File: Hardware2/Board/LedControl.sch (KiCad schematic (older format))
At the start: 47 parts, among them J2 Jumper, J3 Jumper, P1 USB_OTG, P10 TP, P11 2059-302, P12 DISPLAY, P13 TP, P14 Conn_01x03, P15 TP, P16 2059-302, P17 2059-302, P18 CONN_01X03, P19 CONN_01X03, P2 TP, P3 TP, P32 TP, P33 TP, P4 TP, P5 2059-302, P6 TP, P7 TP, P8 Micro_SD, P9 TP, SW1 PEC12R-4215F-S0024, SW2 PEC12R-4215F-S0024, U1 STM32L433CCUx, U2 SP485CN, U3 SP485CN, U4 SP485CN, X1 IQXO/7X

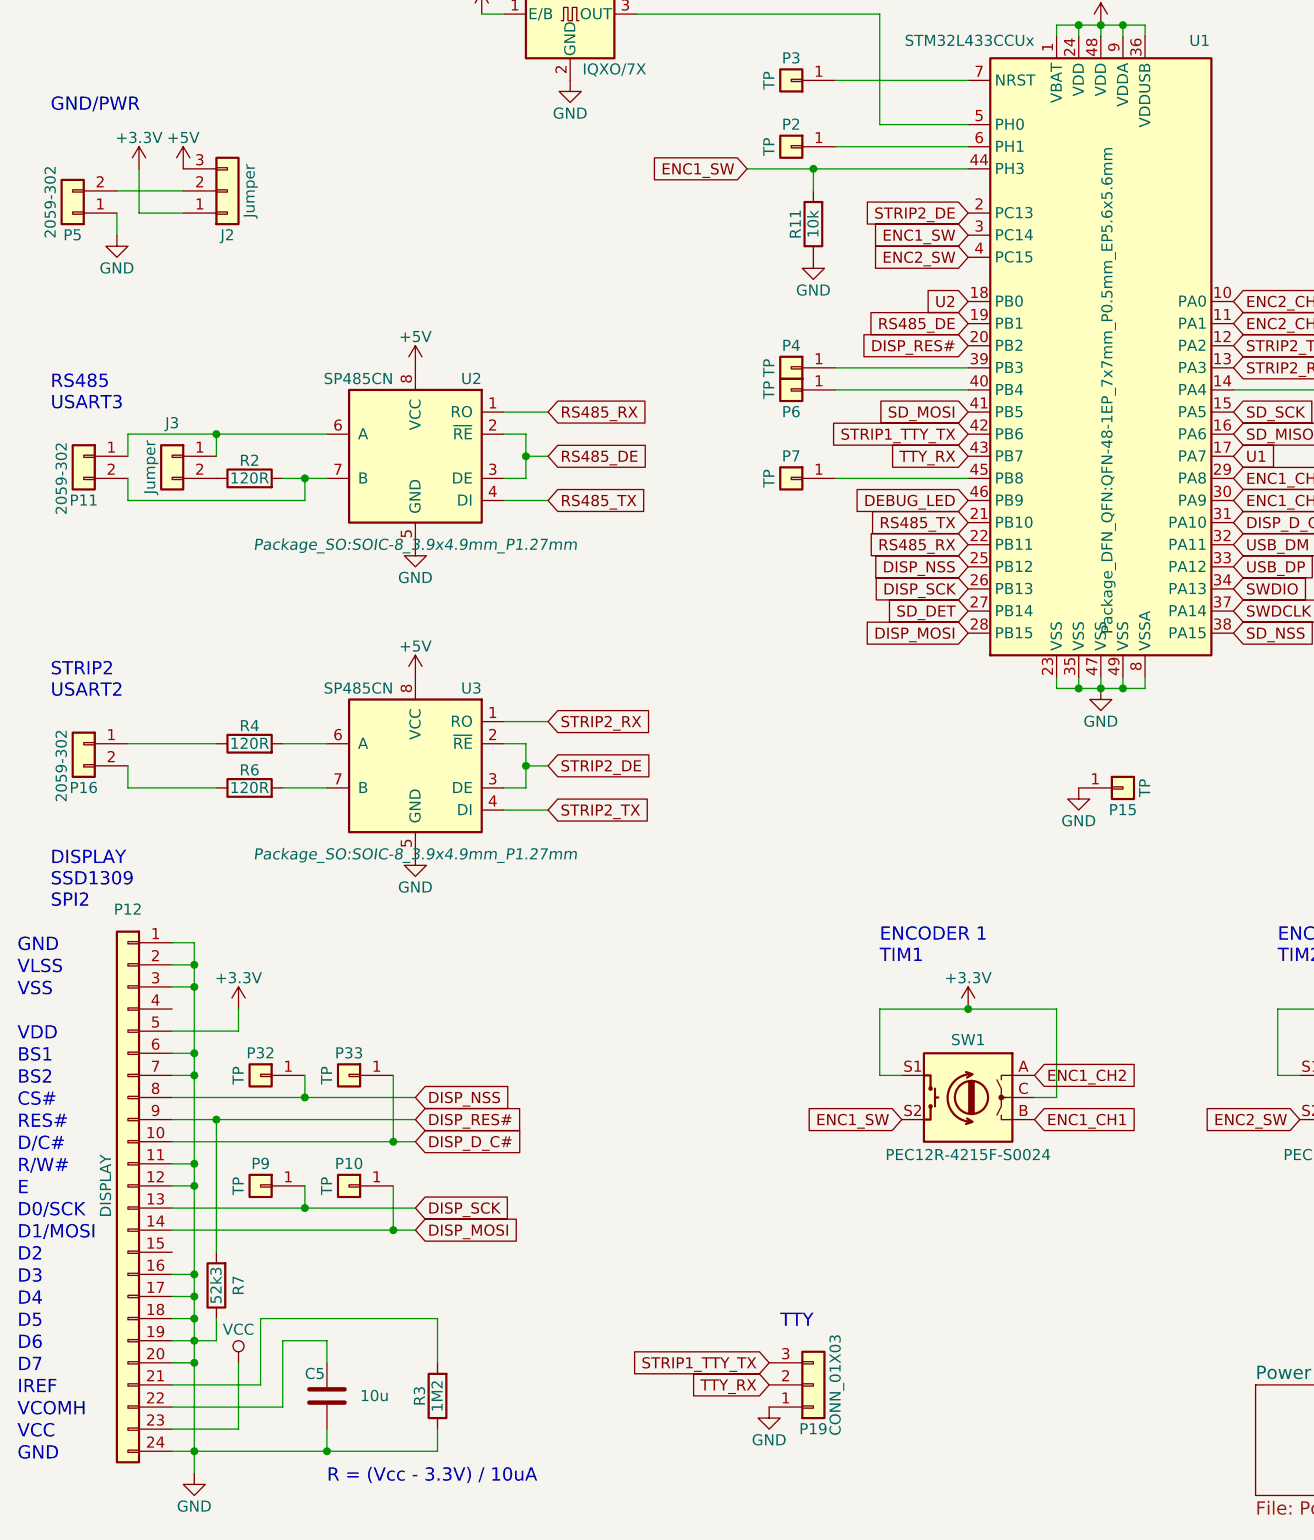
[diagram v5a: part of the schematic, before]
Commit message: Board is ready for production, needs last review
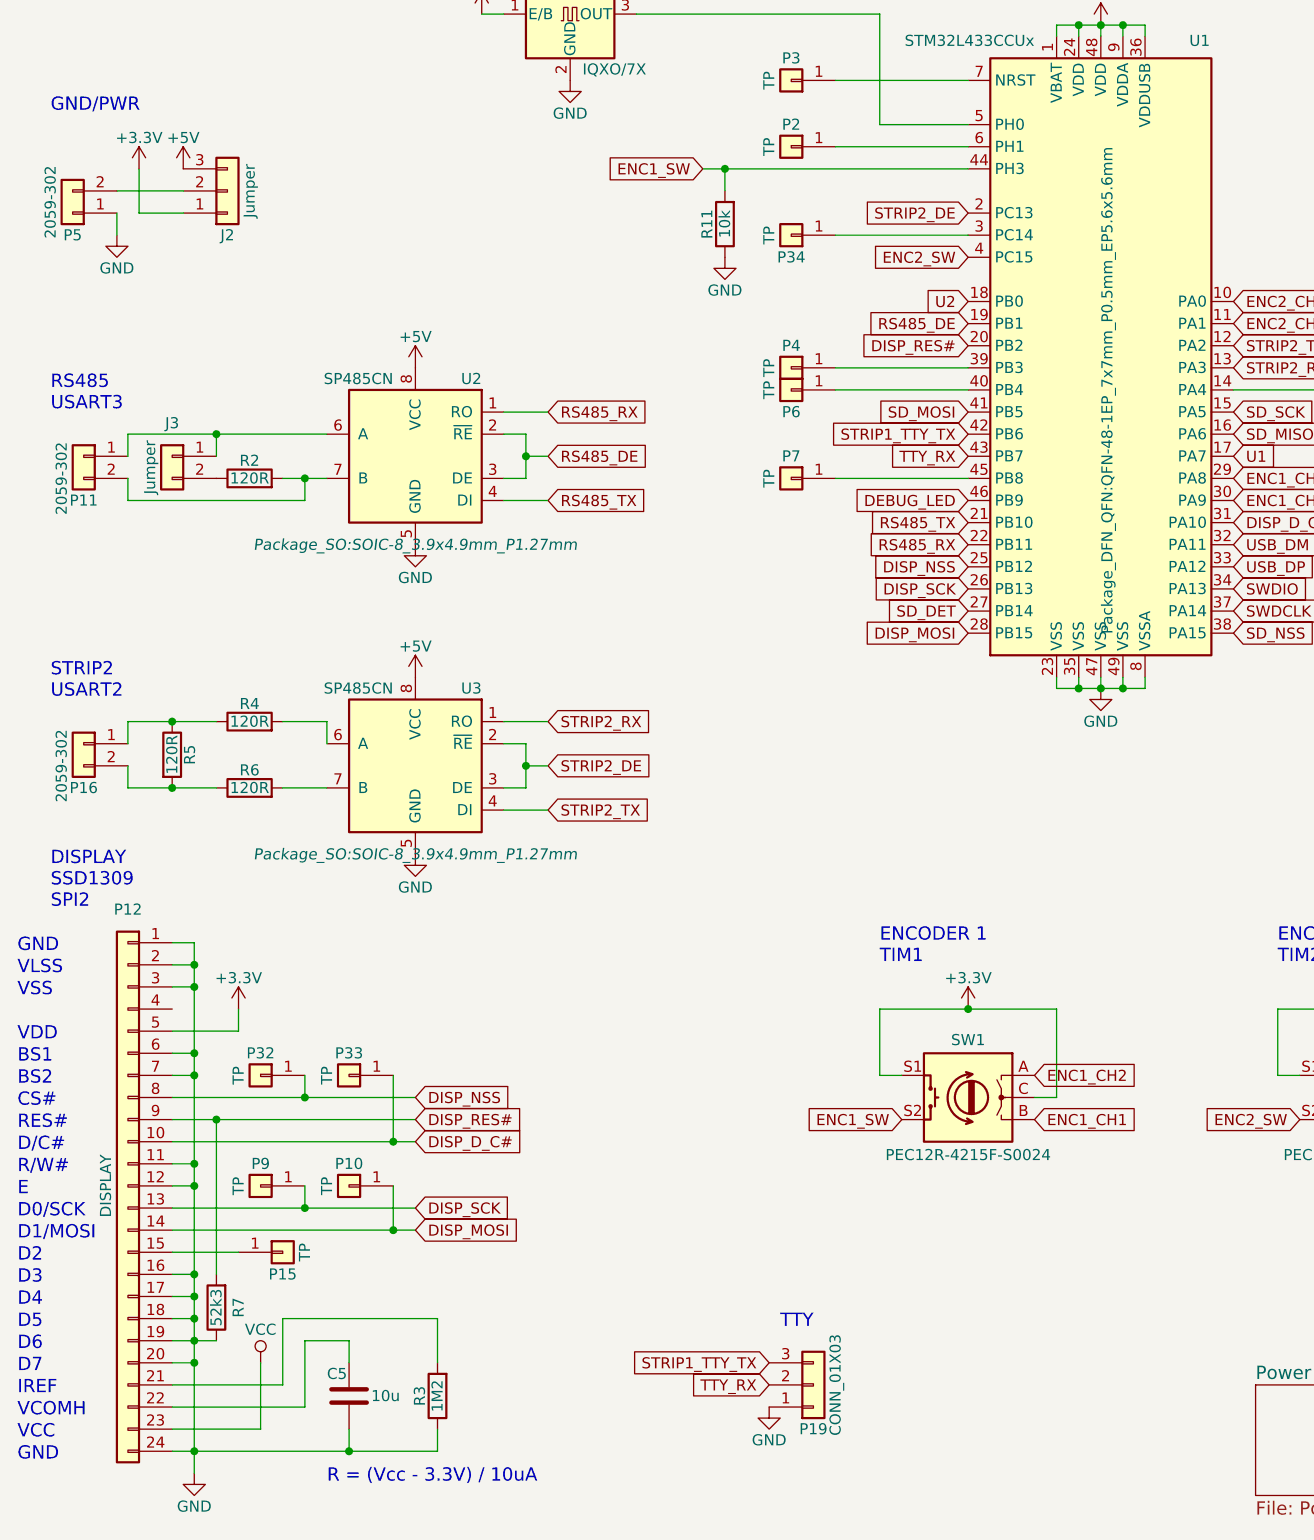
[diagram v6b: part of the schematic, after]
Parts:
- added P34: TP, LedControl:Pad, symbol Connector_Generic:Conn_01x01
- added R5: 120R, Resistor_SMD:R_1206_3216Metric, symbol Device:R
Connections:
- net ENC1_SW: no longer U1.3 (PC14)
- net GND: no longer P15.1 (Pin_1)
- net at P12.15 (Pin_15): now also P15.1 (Pin_1)
- net at P16.1 (Pin_1), R4.1: now also R5.1
- net at P16.2 (Pin_2), R6.1: now also R5.2
- new net: P34.1 (Pin_1), U1.3 (PC14)
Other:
- moved on the sheet: C5, P15, R11, R4, R7
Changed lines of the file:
@@
 L Device:C C5
 U 1 1 58DE3BE4
-P 1900 7250
-F 0 "C5" H 1800 7350 50  0000 L CNN
-F 1 "10u" H 2050 7250 50  0000 L CNN
-F 2 "Capacitor_SMD:C_1206_3216Metric" H 1938 7100 50  0001 C CNN
-F 3 "" H 1900 7250 50  0000 C CNN
-	1    1900 7250
+P 2000 7250
+F 0 "C5" H 1900 7350 50  0000 L CNN
+F 1 "10u" H 2100 7250 50  0000 L CNN
+F 2 "Capacitor_SMD:C_1206_3216Metric" H 2038 7100 50  0001 C CNN
+F 3 "" H 2000 7250 50  0000 C CNN
+	1    2000 7250
 	1    0    0    -1
 $EndComp
@@
 L Device:R R11
 U 1 1 593B2B9C
-P 4100 1950
-F 0 "R11" V 4180 1950 50  0000 C CNN
-F 1 "10k" V 4100 1950 50  0000 C CNN
-F 2 "Resistor_SMD:R_0603_1608Metric" V 4030 1950 50  0001 C CNN
-F 3 "" H 4100 1950 50  0000 C CNN
-	1    4100 1950
+P 3700 1950
+F 0 "R11" V 3780 1950 50  0000 C CNN
+F 1 "10k" V 3700 1950 50  0000 C CNN
+F 2 "Resistor_SMD:R_0603_1608Metric" V 3630 1950 50  0001 C CNN
+F 3 "" H 3700 1950 50  0000 C CNN
+	1    3700 1950
 	-1   0    0    1
 $EndComp
@@
 L power:GND #PWR014
 U 1 1 593B2C10
-P 4100 2100
-F 0 "#PWR014" H 4100 1850 50  0001 C CNN
-F 1 "GND" H 4100 1950 50  0000 C CNN
-F 2 "" H 4100 2100 50  0000 C CNN
-F 3 "" H 4100 2100 50  0000 C CNN
-	1    4100 2100
+P 3700 2100
+F 0 "#PWR014" H 3700 1850 50  0001 C CNN
+F 1 "GND" H 3700 1950 50  0000 C CNN
+F 2 "" H 3700 2100 50  0000 C CNN
+F 3 "" H 3700 2100 50  0000 C CNN
+	1    3700 2100
 	1    0    0    -1
 $EndComp
@@
 L power:VCC #PWR019
 U 1 1 5A627598
-P 1500 7100
-F 0 "#PWR019" H 1500 6950 50  0001 C CNN
-F 1 "VCC" H 1500 7250 50  0000 C CNN
-F 2 "" H 1500 7100 50  0000 C CNN
-F 3 "" H 1500 7100 50  0000 C CNN
-	1    1500 7100
+P 1600 7100
+F 0 "#PWR019" H 1600 6950 50  0001 C CNN
+F 1 "VCC" H 1600 7250 50  0000 C CNN
+F 2 "" H 1600 7100 50  0000 C CNN
+F 3 "" H 1600 7100 50  0000 C CNN
+	1    1600 7100
 	1    0    0    -1
 $EndComp
@@
 L Device:R R7
 U 1 1 5A64B908
-P 1400 6750
-F 0 "R7" V 1300 6750 50  0000 C CNN
-F 1 "52k3" V 1400 6750 50  0000 C CNN
-F 2 "Resistor_SMD:R_0603_1608Metric" V 1330 6750 50  0001 C CNN
-F 3 "" H 1400 6750 50  0000 C CNN
-	1    1400 6750
+P 1400 6850
+F 0 "R7" V 1300 6850 50  0000 C CNN
+F 1 "52k3" V 1400 6850 50  0000 C CNN
+F 2 "Resistor_SMD:R_0603_1608Metric" V 1330 6850 50  0001 C CNN
+F 3 "" H 1400 6850 50  0000 C CNN
+	1    1400 6850
 	-1   0    0    1
 $EndComp
@@
 L Connector_Generic:Conn_01x01 P15
 U 1 1 5A772658
-P 5500 4500
-F 0 "P15" H 5500 4400 50  0000 C CNN
-F 1 "TP" V 5600 4500 50  0000 C CNN
-F 2 "LedControl:Pad" H 5500 4500 50  0001 C CNN
-F 3 "" H 5500 4500 50  0000 C CNN
-	1    5500 4500
+P 1700 6600
+F 0 "P15" H 1700 6500 50  0000 C CNN
+F 1 "TP" V 1800 6600 50  0000 C CNN
+F 2 "LedControl:Pad" H 1700 6600 50  0001 C CNN
+F 3 "" H 1700 6600 50  0000 C CNN
+	1    1700 6600
 	1    0    0    -1
 $EndComp
@@
 L Device:R R4
 U 1 1 5AA88004
-P 1550 4300
-F 0 "R4" V 1630 4300 50  0000 C CNN
-F 1 "120R" V 1550 4300 50  0000 C CNN
-F 2 "Resistor_SMD:R_1206_3216Metric" V 1480 4300 50  0001 C CNN
-F 3 "" H 1550 4300 50  0000 C CNN
-	1    1550 4300
+P 1550 4200
+F 0 "R4" V 1630 4200 50  0000 C CNN
+F 1 "120R" V 1550 4200 50  0000 C CNN
+F 2 "Resistor_SMD:R_1206_3216Metric" V 1480 4200 50  0001 C CNN
+F 3 "" H 1550 4200 50  0000 C CNN
+	1    1550 4200
 	0    -1   -1   0
 $EndComp
-Wire Wire Line
-	1000 4300 1400 4300
-Wire Wire Line
-	1700 4300 1900 4300
 $Comp
 L Device:LED D1
@@
 	1500 5600 1500 5500
 Wire Wire Line
-	1200 7400 1500 7400
-Wire Wire Line
-	1500 7400 1500 7100
-Wire Wire Line
-	1900 7500 1900 7400
-Wire Wire Line
-	1200 7300 1700 7300
-Wire Wire Line
-	1700 7300 1700 7000
-Wire Wire Line
-	1700 7000 1900 7000
-Wire Wire Line
-	1900 7000 1900 7100
-Wire Wire Line
-	1200 7200 1600 7200
-Wire Wire Line
-	1600 7200 1600 6900
+	1200 7400 1600 7400
+Wire Wire Line
+	1600 7400 1600 7100
+Wire Wire Line
+	2000 7500 2000 7400
+Wire Wire Line
+	1200 7300 1800 7300
+Wire Wire Line
+	1800 7300 1800 7000
+Wire Wire Line
+	1800 7000 2000 7000
+Wire Wire Line
+	2000 7000 2000 7100
+Wire Wire Line
+	1200 7200 1700 7200
+Wire Wire Line
+	1700 7200 1700 6900
 Wire Wire Line
 	2400 7500 2400 7400
-Connection ~ 1900 7500
+Connection ~ 2000 7500
 Wire Wire Line
 	1200 6500 2200 6500
@@
 Connection ~ 1300 6700
 Wire Wire Line
-	1600 6900 2400 6900
+	1700 6900 2400 6900
 Wire Wire Line
 	2400 6900 2400 7100
@@
 	1300 7500 1300 7600
 Wire Wire Line
-	1300 7500 1900 7500
+	1300 7500 2000 7500
 Wire Wire Line
 	1300 7100 1300 7500
@@
 	1300 5400 1300 5700
 Wire Wire Line
-	1900 7500 2400 7500
+	2000 7500 2400 7500
 Wire Wire Line
 	8500 1200 9100 1200
@@
 	1800 3100 1900 3100
 Wire Wire Line
-	1400 4500 1000 4500
+	1400 4500 1200 4500
 Wire Wire Line
 	1000 4500 1000 4400
@@
 Text GLabel 4800 1900 0    50   Input ~ 0
 STRIP2_DE
-Text GLabel 4800 2000 0    50   Input ~ 0
-ENC1_SW
 Text GLabel 4800 2100 0    50   Input ~ 0
 ENC2_SW
@@
 Text GLabel 4500 6000 0    50   Input ~ 0
 ENC1_SW
-Text GLabel 3800 1700 0    50   Input ~ 0
+Text GLabel 3600 1700 0    50   Input ~ 0
 ENC1_SW
 Wire Wire Line
-	4800 1700 4100 1700
-Wire Wire Line
-	4100 1800 4100 1700
-Connection ~ 4100 1700
-Wire Wire Line
-	4100 1700 3800 1700
+	4800 1700 3700 1700
+Wire Wire Line
+	3700 1800 3700 1700
+Connection ~ 3700 1700
+Wire Wire Line
+	3700 1700 3600 1700
 Text GLabel 3900 7100 0    50   Input ~ 0
 STRIP1_TTY_TX
@@
 ENC1_CH2
 Wire Wire Line
-	1400 6900 1400 7000
-Wire Wire Line
 	1400 7000 1300 7000
 Wire Wire Line
-	1400 6600 1400 6000
+	1400 6700 1400 6000
 Text GLabel 2300 6500 2    50   Input ~ 0
 DISP_MOSI
@@
 Text GLabel 9100 4300 0    50   Input ~ 0
 SWDIO
-$Comp
-L power:GND #PWR0102
-U 1 1 5C6E9498
-P 5300 4500
-F 0 "#PWR0102" H 5300 4250 50  0001 C CNN
-F 1 "GND" H 5300 4350 50  0000 C CNN
-F 2 "" H 5300 4500 50  0000 C CNN
-F 3 "" H 5300 4500 50  0000 C CNN
-	1    5300 4500
-	1    0    0    -1
-$EndComp
 $Comp
 L Device:D D4
@@
 $EndComp
 Connection ~ 9400 1600
+Wire Wire Line
+	1500 6600 1200 6600
+$Comp
+L Connector_Generic:Conn_01x01 P34
+U 1 1 5C7565CF
+P 4000 2000
+F 0 "P34" H 4000 2100 50  0000 C CNN
+F 1 "TP" V 4100 2000 50  0000 C CNN
+F 2 "LedControl:Pad" H 4000 2000 50  0001 C CNN
+F 3 "" H 4000 2000 50  0000 C CNN
+	1    4000 2000
+	-1   0    0    1
+$EndComp
+Wire Wire Line
+	4200 2000 4800 2000
+$Comp
+L Device:R R5
+U 1 1 5C77FBE7
+P 1200 4350
+F 0 "R5" V 1280 4350 50  0000 C CNN
+F 1 "120R" V 1200 4350 50  0000 C CNN
+F 2 "Resistor_SMD:R_1206_3216Metric" V 1130 4350 50  0001 C CNN
+F 3 "" H 1200 4350 50  0000 C CNN
+	1    1200 4350
+	1    0    0    -1
+$EndComp
+Connection ~ 1200 4500
+Wire Wire Line
+	1200 4500 1000 4500
+Wire Wire Line
+	1000 4300 1000 4200
+Wire Wire Line
+	1000 4200 1200 4200
+Wire Wire Line
+	1200 4200 1400 4200
+Connection ~ 1200 4200
+Wire Wire Line
+	1700 4200 1900 4200
+Wire Wire Line
+	1900 4200 1900 4300
 $EndSCHEMATC
